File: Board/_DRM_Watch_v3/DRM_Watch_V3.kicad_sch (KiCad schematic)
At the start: 112 parts, among them J1 TYPE-C-31-M-12, J2 FPC 10pin 0.5mm pitch, M1 M1.2 screw mount get from DJI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, M2 M1.2 screw mount get from DJI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, M3 M1.2 screw mount get from DJI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, Q1 2N7002LT1G (SOT-23-3), Q2 2N7002LT1G, U1 ESP32-S2, U2 ME6211 SOT23-5 3.3V, U3 TP4056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

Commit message: 2024-04-17 Доповнено схему
2024-04-17 Доповнено схему
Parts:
- D1: value LED TOP -> LED RED; Role (none) -> LED TOP; now in the parts list
- D5: value LED STATUS -> LED BLUE; Role (none) -> LED STATUS; now in the parts list
- J1: Role (none) -> USB Port for charging and update
- Q2: value 2N7002LT1G -> 2N7002LT1G (SOT-23-3); Check_prices https://www.snapeda.com/parts/2N7002LT1G/Onsemi/view-part/?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 -> (none); Link (none) -> https://www.aliexpress.us/item/1005003909614901.html; Link2 (none) -> https://www.aliexpress.us/item/1005003079655220.html; MANUFACTURER ON Semiconductor -> (none); MAXIMUM_PACKAGE_HEIGHT 1.11 mm -> (none); MF onsemi -> (none); MP 2N7002LT1G -> (none); Manufacturer (none) -> ON Semiconductor; PARTREV 4 -> (none); Package SOT-23-3 ON Semiconductor -> (none); Purchase-URL https://www.snapeda.com/api/url_track_click_mouser/?unipart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 -> (none); RS_Components_1032941_Purchase_URL https://www.snapeda.com/api/url_track_click/https%253A//uk.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 -> (none); RS_Components_5450012P_Purchase_URL https://www.snapeda.com/api/url_track_click/https%253A//uk.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 -> (none); RS_Components_5450012_Purchase_URL https://www.snapeda.com/api/url_track_click/https%253A//uk.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 -> (none); Role (none) -> Driving MOSFET for Vibro; STANDARD IPC 7351B -> (none); SnapEDA_Link https://www.snapeda.com/parts/2N7002LT1G/Onsemi/view-part/?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 -> (none); now in the parts list
- R10, R5, R6: Role (none) -> Current limiting resistor for LED
- R17, R18: Role (none) -> Complementary part for EL Driver IC
- R2, R3: Role (none) -> USB Type-C CC Line terminator
- U5: Role (none) -> EL Backlight driver IC

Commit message: 2024-04-18 Оновлено схему 2024-04-18 Оновлено Плату 2024-04-18 Оновлено Production файли для плати rev4
2024-04-18 Оновлено схему
2024-04-18 Оновлено Плату
2024-04-18 Оновлено Production файли для плати rev4
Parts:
- D7: Role (none) -> Catch for backdrop of vibro
- R22: Role (none) -> Step-Down for Vibro Signal
- R23: Role (none) -> Current limit for vibro
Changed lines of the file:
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@@
   )
   (rectangle (start 248.92 210.82) (end 292.1 274.32)
-    (stroke (width 0) (type dash) (color 132 132 132 1))
-    (fill (type none))
+    (stroke (width 0) (type dash) (color 0 194 194 1))
+    (fill (type color) (color 255 255 255 1))
   )
   (rectangle (start 339.09 77.47) (end 391.16 133.35)
     (stroke (width 0) (type dash) (color 0 194 194 1))
-    (fill (type none))
+    (fill (type color) (color 255 255 255 1))
   )
   (rectangle (start 344.17 137.16) (end 400.05 181.61)
@@
   (rectangle (start 20.32 119.38) (end 119.38 176.53)
     (stroke (width 0) (type dash) (color 0 194 194 1))
-    (fill (type none))
+    (fill (type color) (color 255 255 255 1))
   )
   (rectangle (start 120.65 210.82) (end 161.29 254)
@@
   )
   (rectangle (start 82.55 210.82) (end 115.57 270.51)
-    (stroke (width 0) (type dash) (color 132 132 132 1))
-    (fill (type none))
+    (stroke (width 0) (type dash) (color 0 194 194 1))
+    (fill (type color) (color 255 255 255 1))
   )
   (rectangle (start 64.77 72.39) (end 100.33 109.22)
@@
   (rectangle (start 38.1 29.21) (end 83.82 66.04)
     (stroke (width 0) (type dash) (color 0 194 194 1))
-    (fill (type none))
+    (fill (type color) (color 255 255 255 1))
   )
   (rectangle (start 326.39 185.42) (end 391.16 237.49)
@@
   (rectangle (start 90.17 13.97) (end 123.19 46.99)
     (stroke (width 0) (type dash) (color 0 194 194 1))
-    (fill (type none))
+    (fill (type color) (color 255 255 255 1))
   )
   (rectangle (start 146.05 161.29) (end 209.55 185.42)
@@
   (rectangle (start 323.85 25.4) (end 400.05 69.85)
     (stroke (width 0) (type dash) (color 0 194 194 1))
-    (fill (type none))
+    (fill (type color) (color 255 255 255 1))
   )
   (rectangle (start 15.24 210.82) (end 78.74 264.16)
-    (stroke (width 0) (type dash) (color 132 132 132 1))
-    (fill (type none))
+    (stroke (width 0) (type dash) (color 0 194 194 1))
+    (fill (type color) (color 255 255 255 1))
   )
   (rectangle (start 166.37 210.82) (end 243.84 274.32)
-    (stroke (width 0) (type dash) (color 132 132 132 1))
-    (fill (type none))
+    (stroke (width 0) (type dash) (color 0 194 194 1))
+    (fill (type color) (color 255 255 255 1))
   )
   (text "MOUNT HOLES" (at 30.48 77.47 0)
@@
     )
     (property "Description" "SMD Resistor" (at 275.59 254 0)
+      (effects (font (size 1.27 1.27)) hide)
+    )
+    (property "Role" "Current limit for vibro" (at 275.59 254 0)
       (effects (font (size 1.27 1.27)) hide)
     )
@@
       (effects (font (size 1.27 1.27)) hide)
     )
+    (property "Role" "Catch for backdrop of vibro" (at 270.51 246.38 0)
+      (effects (font (size 1.27 1.27)) hide)
+    )
     (pin "1")
     (pin "2")
@@
       (effects (font (size 1.27 1.27)) hide)
     )
+    (property "Role" "Step-Down for Vibro Signal" (at 256.54 261.62 0)
+      (effects (font (size 1.27 1.27)) hide)
+    )
     (pin "1")
     (pin "2")
@@
       (effects (font (size 1.27 1.27)) hide)
     )
-    (property "Description" "" (at 91.44 157.48 90)
+    (property "Description" "SMD 0805 Red LED" (at 91.44 157.48 90)
       (effects (font (size 1.27 1.27)) hide)
     )
@@
       (effects (font (size 1.27 1.27)) hide)
     )
-    (property "Description" "" (at 92.71 144.78 90)
+    (property "Description" "SMD 0805 Blue LED" (at 92.71 144.78 90)
       (effects (font (size 1.27 1.27)) hide)
     )
@@
       (effects (font (size 1.27 1.27)) hide)
     )
-    (property "Description" "" (at 46.99 49.53 0)
+    (property "Description" "Unpolarized Capacitor" (at 46.99 49.53 0)
       (effects (font (size 1.27 1.27)) hide)
     )
@@
       (effects (font (size 1.27 1.27)) hide)
     )
-    (property "Description" "" (at 101.6 31.75 0)
-      (effects (font (size 1.27 1.27)) hide)
-    )
+    (property "Description" "Unpolarized capacitor" (at 101.6 31.75 0)
+      (effects (font (size 1.27 1.27)) hide)
+    )

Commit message: 2024-06-22 v2.32  Збільшено кількість точок що додаються на один кадр 2024-06-22 v2.32  Реалізовано: Перед вимкненням по таймеру щоб ліхтар мигав щосекунди 2024-06-22 v2.32  Реалізовано: якщо годинник в глибокому розряді - не стартувати а відправлятись одразу в сон 2024-06-22 v2.32  Додана мелодія: Angry birds 2024-06-22 v2.32  Доповнено документацію
2024-06-22 v2.32  Збільшено кількість точок що додаються на один кадр
2024-06-22 v2.32  Реалізовано: Перед вимкненням по таймеру щоб ліхтар мигав щосекунди
2024-06-22 v2.32  Реалізовано: якщо годинник в глибокому розряді - не стартувати а відправлятись одразу в сон
2024-06-22 v2.32  Додана мелодія: Angry birds
2024-06-22 v2.32  Доповнено документацію
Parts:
- R9: value 10K -> 2K
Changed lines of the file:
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@@
       (effects (font (size 1.27 1.27) bold) (justify left))
     )
-    (property "Value" "10K" (at 29.21 142.24 0)
+    (property "Value" "2K" (at 29.21 142.24 0)
       (effects (font (size 1.27 1.27)) (justify left))
     )

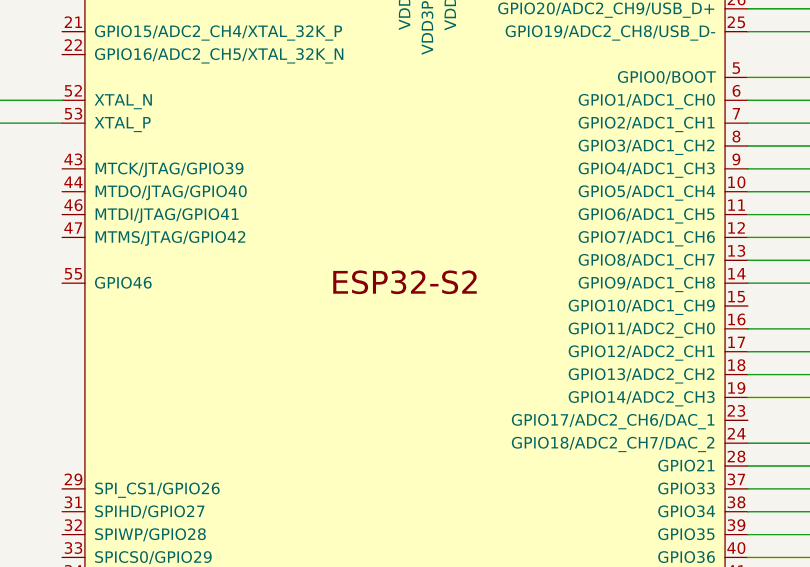
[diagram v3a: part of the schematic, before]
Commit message: 2024-06-29 v2.33  Виправлено помилку - тип мікросхеми в схемі і на платі 2024-06-29 v2.33  Дописано флешер для Windows 2024-06-29 v2.33  Доповнено документацію
2024-06-29 v2.33  Виправлено помилку - тип мікросхеми в схемі і на платі
2024-06-29 v2.33  Дописано флешер для Windows
2024-06-29 v2.33  Доповнено документацію
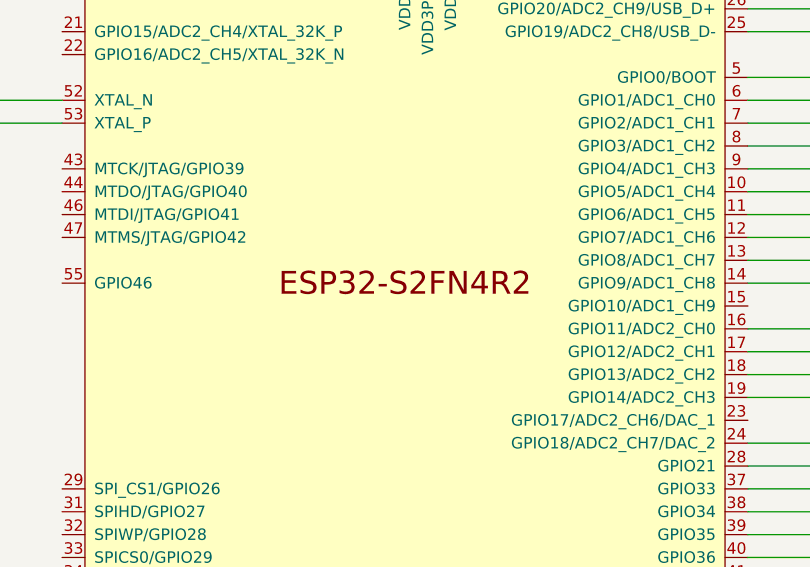
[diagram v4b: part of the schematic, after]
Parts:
- U1: value ESP32-S2 -> ESP32-S2FN4R2
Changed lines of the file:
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@@
       (effects (font (size 1.27 1.27)) (justify left) hide)
     )
-    (property "Value" "ESP32-S2" (at 181.2641 156.21 0)
+    (property "Value" "ESP32-S2FN4R2" (at 181.2641 156.21 0)
       (effects (font (size 1.27 1.27)) (justify left) hide)
     )
@@
       (effects (font (size 1.27 1.27)) hide)
     )
-    (property "Description" "ESP32-S2 Programmable Microcontroller Chip" (at 179.07 110.49 0)
+    (property "Description" "ESP32-S2FN4R2 Programmable Microcontroller Chip" (at 179.07 110.49 0)
       (effects (font (size 1.27 1.27)) hide)
     )

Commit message: 2024-06-29 v2.33  В схемі виправлено хибне посилання на невірний кварц
2024-06-29 v2.33  В схемі виправлено хибне посилання на невірний кварц
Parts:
- Y1: footprint Project-Lib:OSC_XRCGB48M000F0Z00R0 -> Project-Lib:Oscilator; symbol Project-Lib:XRCGB48M000F0Z00R0 -> Project-Lib:Oscolator; Manufacturer Murata Electronics -> (none)
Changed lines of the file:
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@@
     )
   )
-  (symbol (lib_id "Project-Lib:XRCGB48M000F0Z00R0") (at 87.63 93.98 270) (mirror x) (unit 1)
+  (symbol (lib_id "Project-Lib:Oscolator") (at 87.63 93.98 270) (mirror x) (unit 1)
     (in_bom yes) (on_board yes) (dnp no)
     (property "Reference" "Y1" (at 87.63 91.44 90)
@@
       (effects (font (face "KiCad Font") (size 0.5 0.5)) (justify left) hide)
     )
-    (property "Footprint" "Project-Lib:OSC_XRCGB48M000F0Z00R0" (at 87.63 93.98 0)
+    (property "Footprint" "Project-Lib:Oscilator" (at 68.58 93.98 0)
       (effects (font (size 1.27 1.27)) (justify bottom) hide)
     )
@@
       (effects (font (size 1.27 1.27)) (justify bottom) hide)
     )
-    (property "Manufacturer" "Murata Electronics" (at 66.04 93.98 0)
-      (effects (font (size 1.27 1.27)) (justify bottom) hide)
-    )

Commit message: 2024-06-30 v2.33  Виправлена інформація про гайки на платі:  Brass SMTSO-M1.4X3X1.5-2X0.8
2024-06-30 v2.33  Виправлена інформація про гайки на платі:  Brass SMTSO-M1.4X3X1.5-2X0.8
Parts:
- M1, M2, M3: value M1.2 screw mount get from DJI Mavic 3 CORE board -> Brass SMTSO-M1.4X3X1.5-2X0.8; footprint Project-Lib:m1.2-screw-mount -> Project-Lib:m1.4-screw-mount; Link https://www.aliexpress.com/i/1005005125674149.html (SMTSO-M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 -> https://www.aliexpress.com/item/1005005579653583.html
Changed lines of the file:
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@@
       (effects (font (size 1.27 1.27) bold) (justify left))
     )
-    (property "Value" "M1.2 screw mount get from DJI Mavic 3 CORE board" (at 34.29 92.71 0)
+    (property "Value" "Brass SMTSO-M1.4X3X1.5-2X0.8" (at 34.29 92.71 0)
       (effects (font (size 1.27 1.27)) hide)
     )
-    (property "Footprint" "Project-Lib:m1.2-screw-mount" (at 34.29 92.71 0)
+    (property "Footprint" "Project-Lib:m1.4-screw-mount" (at 34.29 92.71 0)
       (effects (font (size 1.27 1.27)) hide)
     )
-    (property "Datasheet" "https://www.swaco.com/SMTSO-M1.2-2ET-PEM-ReelFast" (at 34.29 92.71 0)
+    (property "Datasheet" "" (at 34.29 92.71 0)
       (effects (font (size 1.27 1.27)) hide)
     )
-    (property "Link" "https://www.aliexpress.com/i/1005005125674149.html   (SMTSO-M1.2-2)" (at 34.29 92.71 0)
+    (property "Link" "https://www.aliexpress.com/item/1005005579653583.html" (at 34.29 92.71 0)
       (effects (font (size 1.27 1.27)) hide)
     )
@@
       (effects (font (size 1.27 1.27)) hide)
     )
-    (property "Description" "Surface mount spacers with thread" (at 34.29 92.71 0)
+    (property "Description" "M1.4 screw mount get from DJI Mavic 3 CORE board" (at 34.29 92.71 0)
       (effects (font (size 1.27 1.27)) hide)
     )
@@
       (effects (font (size 1.27 1.27) bold) (justify left))
     )
-    (property "Value" "M1.2 screw mount get from DJI Mavic 3 CORE board" (at 34.29 77.47 0)
+    (property "Value" "Brass SMTSO-M1.4X3X1.5-2X0.8" (at 34.29 77.47 0)
       (effects (font (size 1.27 1.27)) hide)
     )
-    (property "Footprint" "Project-Lib:m1.2-screw-mount" (at 34.29 77.47 0)
+    (property "Footprint" "Project-Lib:m1.4-screw-mount" (at 34.29 77.47 0)
       (effects (font (size 1.27 1.27)) hide)
     )
-    (property "Datasheet" "https://www.swaco.com/SMTSO-M1.2-2ET-PEM-ReelFast" (at 34.29 77.47 0)
+    (property "Datasheet" "" (at 34.29 77.47 0)
       (effects (font (size 1.27 1.27)) hide)
     )
-    (property "Link" "https://www.aliexpress.com/i/1005005125674149.html   (SMTSO-M1.2-2)" (at 34.29 77.47 0)
+    (property "Link" "https://www.aliexpress.com/item/1005005579653583.html" (at 34.29 77.47 0)
       (effects (font (size 1.27 1.27)) hide)
     )
@@
       (effects (font (size 1.27 1.27)) hide)
     )
-    (property "Description" "Surface mount spacers with thread" (at 34.29 77.47 0)
+    (property "Description" "M1.4 screw mount get from DJI Mavic 3 CORE board" (at 34.29 77.47 0)
       (effects (font (size 1.27 1.27)) hide)
     )
@@
       (effects (font (size 1.27 1.27) bold) (justify left))
     )
-    (property "Value" "M1.2 screw mount get from DJI Mavic 3 CORE board" (at 34.29 85.09 0)
+    (property "Value" "Brass SMTSO-M1.4X3X1.5-2X0.8" (at 34.29 85.09 0)
       (effects (font (size 1.27 1.27)) hide)
     )
-    (property "Footprint" "Project-Lib:m1.2-screw-mount" (at 34.29 85.09 0)
+    (property "Footprint" "Project-Lib:m1.4-screw-mount" (at 34.29 85.09 0)
       (effects (font (size 1.27 1.27)) hide)
     )
-    (property "Datasheet" "https://www.swaco.com/SMTSO-M1.2-2ET-PEM-ReelFast" (at 34.29 85.09 0)
+    (property "Datasheet" "" (at 34.29 85.09 0)
       (effects (font (size 1.27 1.27)) hide)
     )
-    (property "Link" "https://www.aliexpress.com/i/1005005125674149.html   (SMTSO-M1.2-2)" (at 34.29 85.09 0)
+    (property "Link" "https://www.aliexpress.com/item/1005005579653583.html" (at 34.29 85.09 0)
       (effects (font (size 1.27 1.27)) hide)
     )
@@
       (effects (font (size 1.27 1.27)) hide)
     )
-    (property "Description" "Surface mount spacers with thread" (at 34.29 85.09 0)
+    (property "Description" "M1.4 screw mount get from DJI Mavic 3 CORE board" (at 34.29 85.09 0)
       (effects (font (size 1.27 1.27)) hide)
     )

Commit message: 2024-07-01  Виправлено посилання Readme на ESP32 2024-07-01  Виправлено посилання Readme на Гайки для пайки 2024-07-01  Виправлено посилання Readme на Гайки для пайки 2024-07-01  Доповнена інформація про заглушки USB 2024-07-01  В схемі оновлена інформація про ESP32
2024-07-01  Виправлено посилання Readme на ESP32
2024-07-01  Виправлено посилання Readme на Гайки для пайки
2024-07-01  Виправлено посилання Readme на Гайки для пайки
2024-07-01  Доповнена інформація про заглушки USB
2024-07-01  В схемі оновлена інформація про ESP32
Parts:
- U1: Link https://www.tme.eu/en/details/esp32s2/iot-wifi-bluetooth-mo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 -> https://www.tme.eu/ua/details/esp32s2fn4r2/moduli-iot-wifi-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
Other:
- title: DRM Watch V3 -> DRM Watch 3
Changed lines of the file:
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@@
   (paper "A3")
   (title_block
-    (title "DRM Watch V3")
-    (date "2023-12-05")
-    (rev "0.1")
+    (title "DRM Watch 3")
+    (date "2024-07-01")
+    (rev "5")
     (company "Dr. Failov")
   )
@@
       (effects (font (size 1.27 1.27)) hide)
     )
-    (property "Link" "https://www.tme.eu/en/details/esp32s2/iot-wifi-bluetooth-modules/espressif/esp32-s2/" (at 179.07 110.49 0)
-      (effects (font (size 1.27 1.27)) hide)
-    )
+    (property "Link" "https://www.tme.eu/ua/details/esp32s2fn4r2/moduli-iot-wifi-bluetooth/espressif/esp32-s2fn4r2" (at 179.07 110.49 0)
+      (effects (font (size 1.27 1.27)) hide)
+    )
